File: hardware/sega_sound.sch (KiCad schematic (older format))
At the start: 9 parts, among them J1 AVR-ISP-6, U1 ATmega8-16PU, U2 SN76489AN

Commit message: added simulation script to firmware for testing
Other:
- note added: "Abblockkondensatoren (U1, U2)"
- note removed: "Abblockkondensatorn (U1, U2)"
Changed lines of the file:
@@
 	1650 1350 1650 1450
 Text Notes 650  600  0    50   ~ 0
-Abblockkondensatorn (U1, U2)
+Abblockkondensatoren (U1, U2)
 Text GLabel 4650 3200 2    50   Output ~ 0
 SOUND_WE

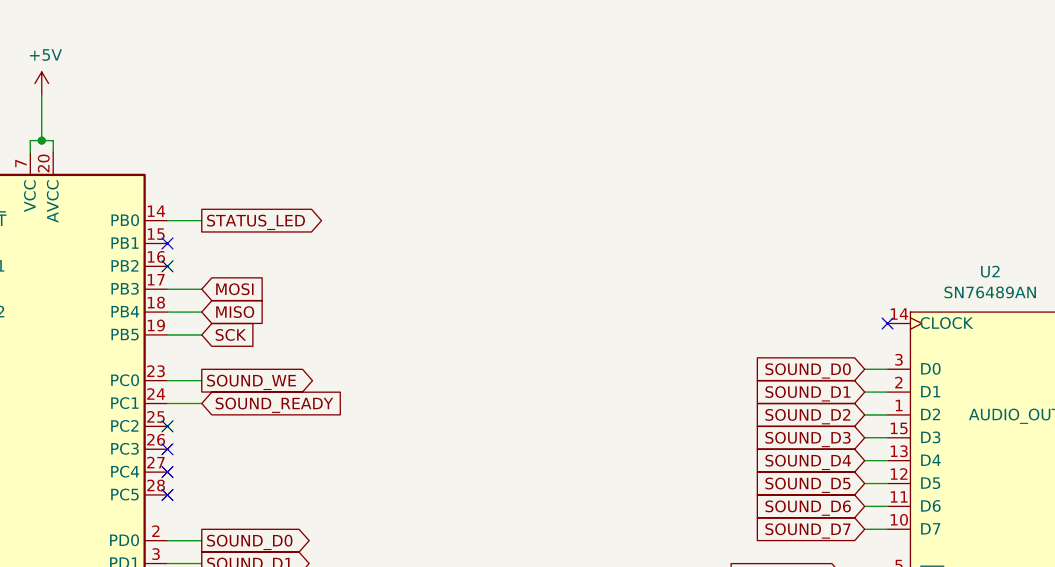
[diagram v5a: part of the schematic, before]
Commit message: added 4mhz clock wire from atmega to sn76489
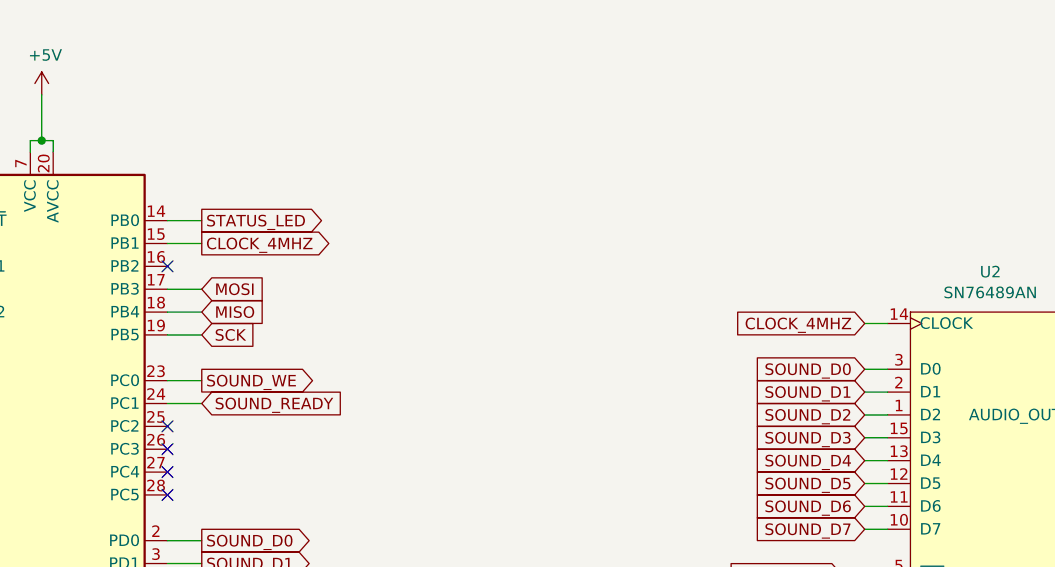
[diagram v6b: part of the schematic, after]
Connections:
- net CLOCK_4MHZ: now reaches U1.15 (PB1)
- net CLOCK_4MHZ: now also U2.14 (CLOCK)
- no-connect marks 10 -> 8
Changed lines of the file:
@@
 Sheet 1 2
 Title "Sega Sound with SN76489AN"
-Date "2020-01-22"
+Date "2020-01-27"
 Rev "1.0"
 Comp "Thorsten Kattanek"
@@
 Text Notes 1200 6000 0    50   ~ 0
 ISP (6 Pin Connector)
-NoConn ~ 4500 2600
 NoConn ~ 4500 2700
 NoConn ~ 4500 3400
@@
 NoConn ~ 3300 2900
 NoConn ~ 3300 2700
-NoConn ~ 7650 2950
 $Comp
 L Device:C C1
@@
 Text Notes 2750 5750 0    50   ~ 0
 System Status LED
+Text GLabel 4650 2600 2    50   Output ~ 0
+CLOCK_4MHZ
+Wire Wire Line
+	4500 2600 4650 2600
+Text GLabel 7550 2950 0    50   Input ~ 0
+CLOCK_4MHZ
+Wire Wire Line
+	7550 2950 7650 2950
 $EndSCHEMATC

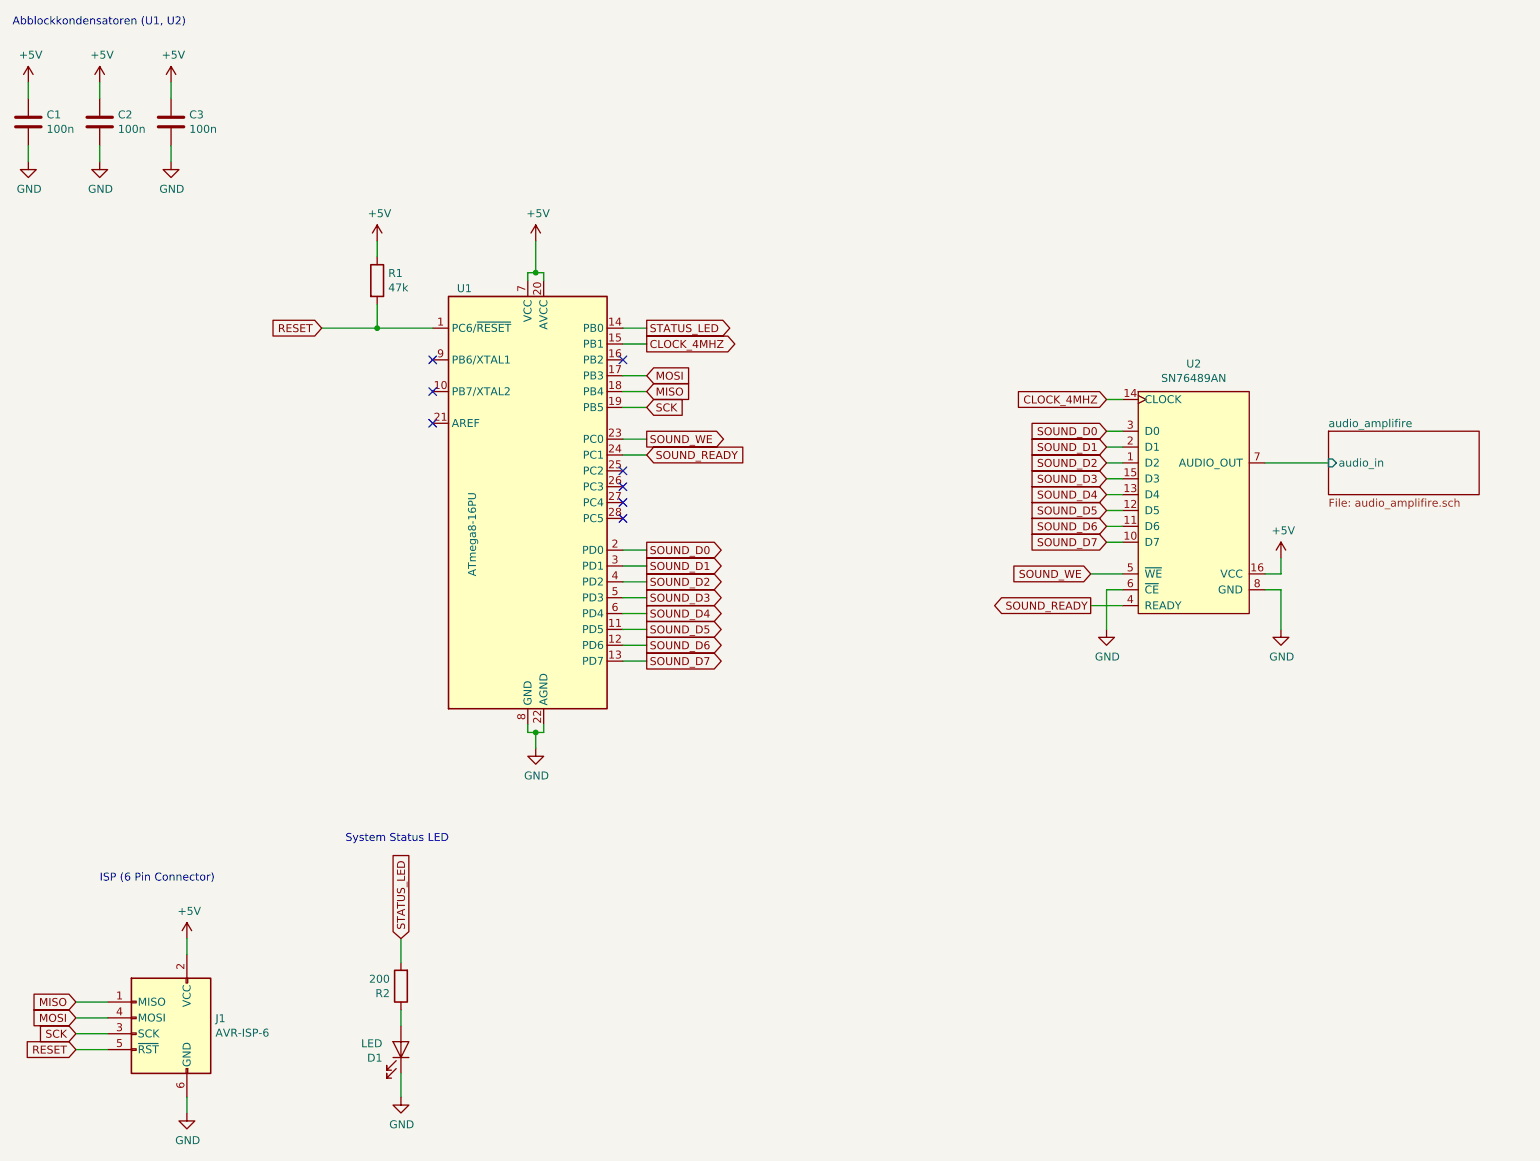
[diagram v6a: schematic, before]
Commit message: hardware: added 10k pullup resistor for ready signal and sort controll wires (ce, we, ready)
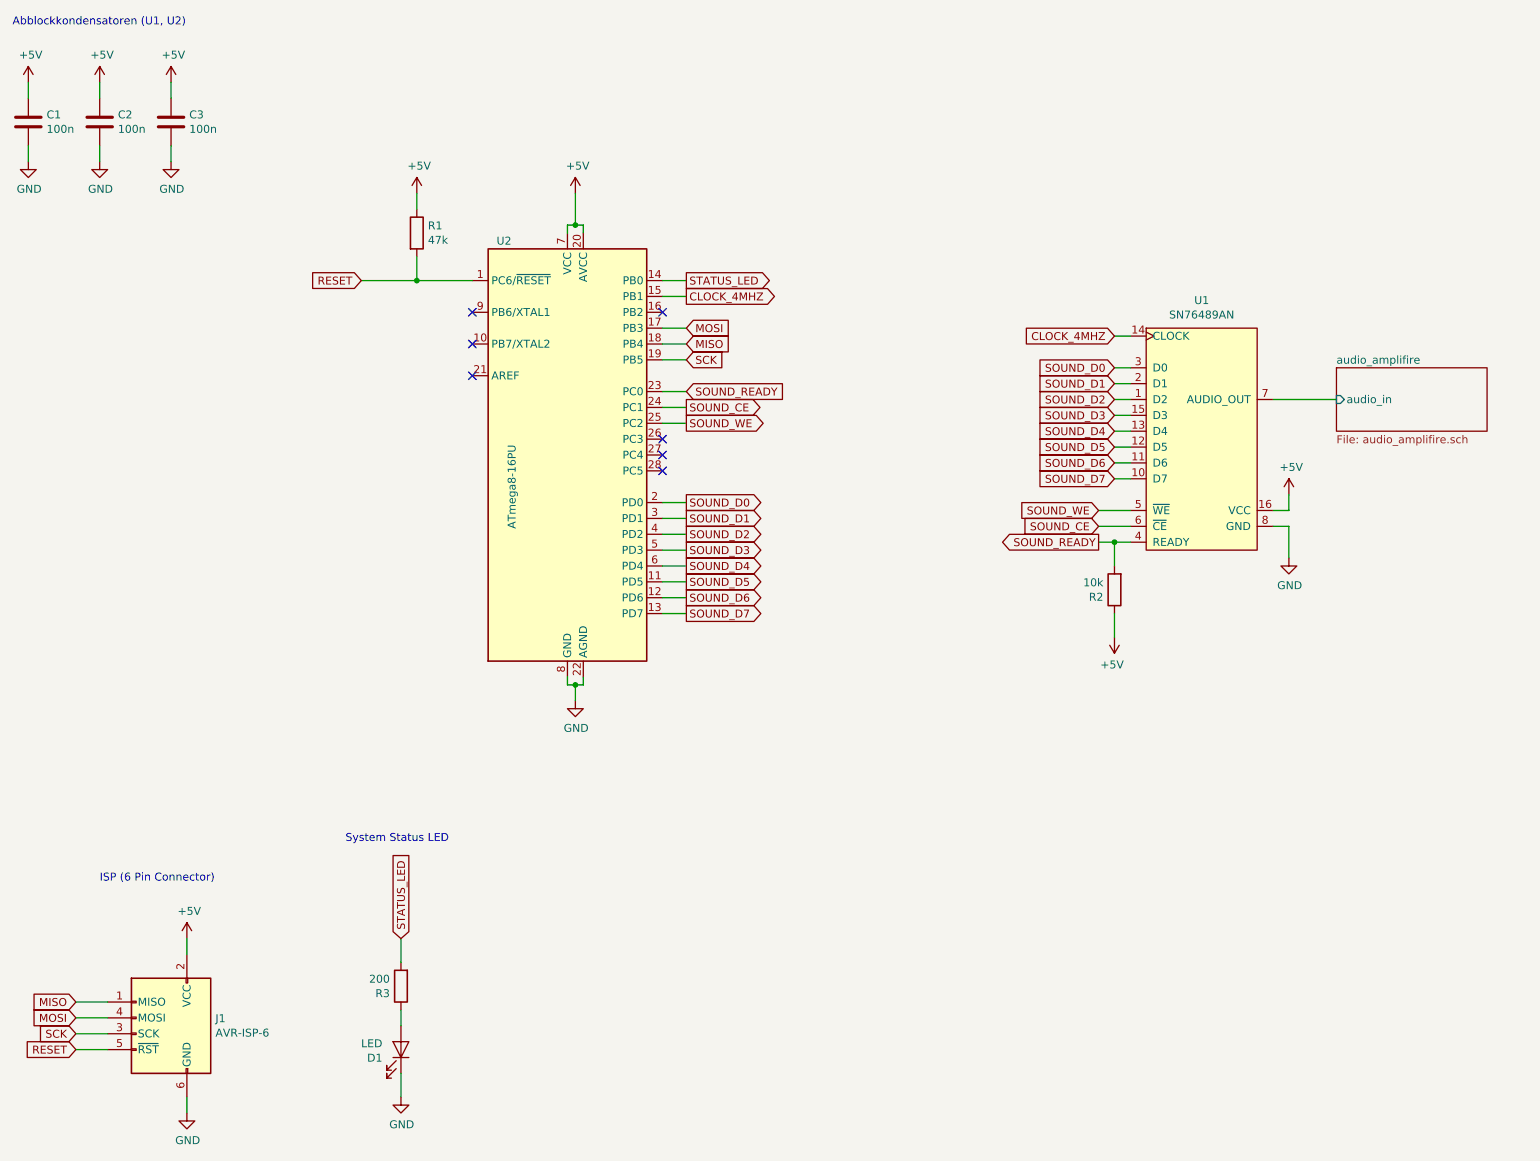
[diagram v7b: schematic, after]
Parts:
- added R2: 10k, symbol Device:R
- renumbered R2 to R3, U2 to U1, U1 to U2
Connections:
- net +5V: now also R2.1
- net GND: no longer U1.6 (~CE)
- net SOUND_READY: now also U2.23 (PC0), R2.2; no longer U2.24 (PC1)
- net SOUND_WE: now also U2.25 (PC2); no longer U2.23 (PC0)
- new net SOUND_CE: U1.6 (~CE), U2.24 (PC1)
- no-connect marks 8 -> 7
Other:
- moved on the sheet: R1, U1, U2

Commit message: hardware: added simply class a audio amplifiere
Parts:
- added J1, J2: Conn_01x02, symbol Connector_Generic:Conn_01x02
- renumbered J1 to J3
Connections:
- net +5V: now also J1.1 (Pin_1)
- net GND: now also J1.2 (Pin_2), J2.2 (Pin_2)
- new net +12V: J2.1 (Pin_1)
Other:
- note added: "12V Einspeisung"
- note added: "5V Einspeisung"
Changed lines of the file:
@@
 $EndComp
 $Comp
-L Connector:AVR-ISP-6 J1
+L Connector:AVR-ISP-6 J3
 U 1 1 5E274AFE
 P 1650 6950
-F 0 "J1" H 1370 7046 50  0000 R CNN
+F 0 "J3" H 1370 7046 50  0000 R CNN
 F 1 "AVR-ISP-6" H 1370 6955 50  0000 R CNN
 F 2 "" V 1400 7000 50  0001 C CNN
@@
 Connection ~ 3200 2200
 $Comp
-L power:+5V #PWR013
+L power:+5V #PWR017
 U 1 1 5E279685
 P 1750 6350
-F 0 "#PWR013" H 1750 6200 50  0001 C CNN
+F 0 "#PWR017" H 1750 6200 50  0001 C CNN
 F 1 "+5V" H 1765 6523 50  0000 C CNN
 F 2 "" H 1750 6350 50  0001 C CNN
@@
 $EndComp
 $Comp
-L power:GND #PWR015
+L power:GND #PWR019
 U 1 1 5E279E4E
 P 1750 7450
-F 0 "#PWR015" H 1750 7200 50  0001 C CNN
+F 0 "#PWR019" H 1750 7200 50  0001 C CNN
 F 1 "GND" H 1755 7277 50  0000 C CNN
 F 2 "" H 1750 7450 50  0001 C CNN
@@
 STATUS_LED
 $Comp
-L power:GND #PWR014
+L power:GND #PWR018
 U 1 1 5E29C499
 P 3100 7350
-F 0 "#PWR014" H 3100 7100 50  0001 C CNN
+F 0 "#PWR018" H 3100 7100 50  0001 C CNN
 F 1 "GND" H 3105 7177 50  0000 C CNN
 F 2 "" H 3100 7350 50  0001 C CNN
@@
 Wire Wire Line
 	7600 4300 7600 4450
+$Comp
+L Connector_Generic:Conn_01x02 J1
+U 1 1 5E3CFD8B
+P 7600 5600
+F 0 "J1" V 7564 5412 50  0000 R CNN
+F 1 "Conn_01x02" V 7473 5412 50  0000 R CNN
+F 2 "" H 7600 5600 50  0001 C CNN
+F 3 "~" H 7600 5600 50  0001 C CNN
+	1    7600 5600
+	0    -1   -1   0
+$EndComp
+$Comp
+L Connector_Generic:Conn_01x02 J2
+U 1 1 5E3D1958
+P 8650 5600
+F 0 "J2" V 8614 5412 50  0000 R CNN
+F 1 "Conn_01x02" V 8523 5412 50  0000 R CNN
+F 2 "" H 8650 5600 50  0001 C CNN
+F 3 "~" H 8650 5600 50  0001 C CNN
+	1    8650 5600
+	0    -1   -1   0
+$EndComp
+$Comp
+L power:GND #PWR016
+U 1 1 5E3D1FA3
+P 8750 5950
+F 0 "#PWR016" H 8750 5700 50  0001 C CNN
+F 1 "GND" H 8755 5777 50  0000 C CNN
+F 2 "" H 8750 5950 50  0001 C CNN
+F 3 "" H 8750 5950 50  0001 C CNN
+	1    8750 5950
+	1    0    0    -1
+$EndComp
+$Comp
+L power:GND #PWR015
+U 1 1 5E3D2F04
+P 7700 5950
+F 0 "#PWR015" H 7700 5700 50  0001 C CNN
+F 1 "GND" H 7705 5777 50  0000 C CNN
+F 2 "" H 7700 5950 50  0001 C CNN
+F 3 "" H 7700 5950 50  0001 C CNN
+	1    7700 5950
+	1    0    0    -1
+$EndComp
+Wire Wire Line
+	8750 5800 8750 5950
+Wire Wire Line
+	7700 5800 7700 5950
+$Comp
+L power:+12V #PWR014
+U 1 1 5E3D615E
+P 8600 5900
+F 0 "#PWR014" H 8600 5750 50  0001 C CNN
+F 1 "+12V" V 8615 6028 50  0000 L CNN
+F 2 "" H 8600 5900 50  0001 C CNN
+F 3 "" H 8600 5900 50  0001 C CNN
+	1    8600 5900
+	0    -1   -1   0
+$EndComp
+$Comp
+L power:+5V #PWR013
+U 1 1 5E3D8780
+P 7550 5900
+F 0 "#PWR013" H 7550 5750 50  0001 C CNN
+F 1 "+5V" H 7565 6073 50  0000 C CNN
+F 2 "" H 7550 5900 50  0001 C CNN
+F 3 "" H 7550 5900 50  0001 C CNN
+	1    7550 5900
+	0    -1   -1   0
+$EndComp
+Wire Wire Line
+	7550 5900 7600 5900
+Wire Wire Line
+	7600 5900 7600 5800
+Wire Wire Line
+	8600 5900 8650 5900
+Wire Wire Line
+	8650 5900 8650 5800
+Text Notes 7350 5400 0    50   ~ 0
+5V Einspeisung
+Text Notes 8400 5400 0    50   ~ 0
+12V Einspeisung
 $EndSCHEMATC
